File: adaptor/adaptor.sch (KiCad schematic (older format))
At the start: 11 parts, among them P1 CONN_1, P2 nRF24l01, P3 ISP, P4 CONN_1, P5 CONN_1, P6 Clock, P7 Out, P8 In, P9 Serial

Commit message: Add power jack and rj45 connectors to adaptor
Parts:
- removed W1: NoOut, symbol TEST
- removed W2: NoIn, symbol TEST
- added J1, J2: RJ45, symbol RJ45
- added JP1: NoOut, symbol JUMPER
- added JP2: NoIn, symbol JUMPER
- added K1: DC Jack, symbol CONN_3
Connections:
- wire segments 62 -> 84
- no-connect marks 2 -> 7
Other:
- moved on the sheet: P7, P8

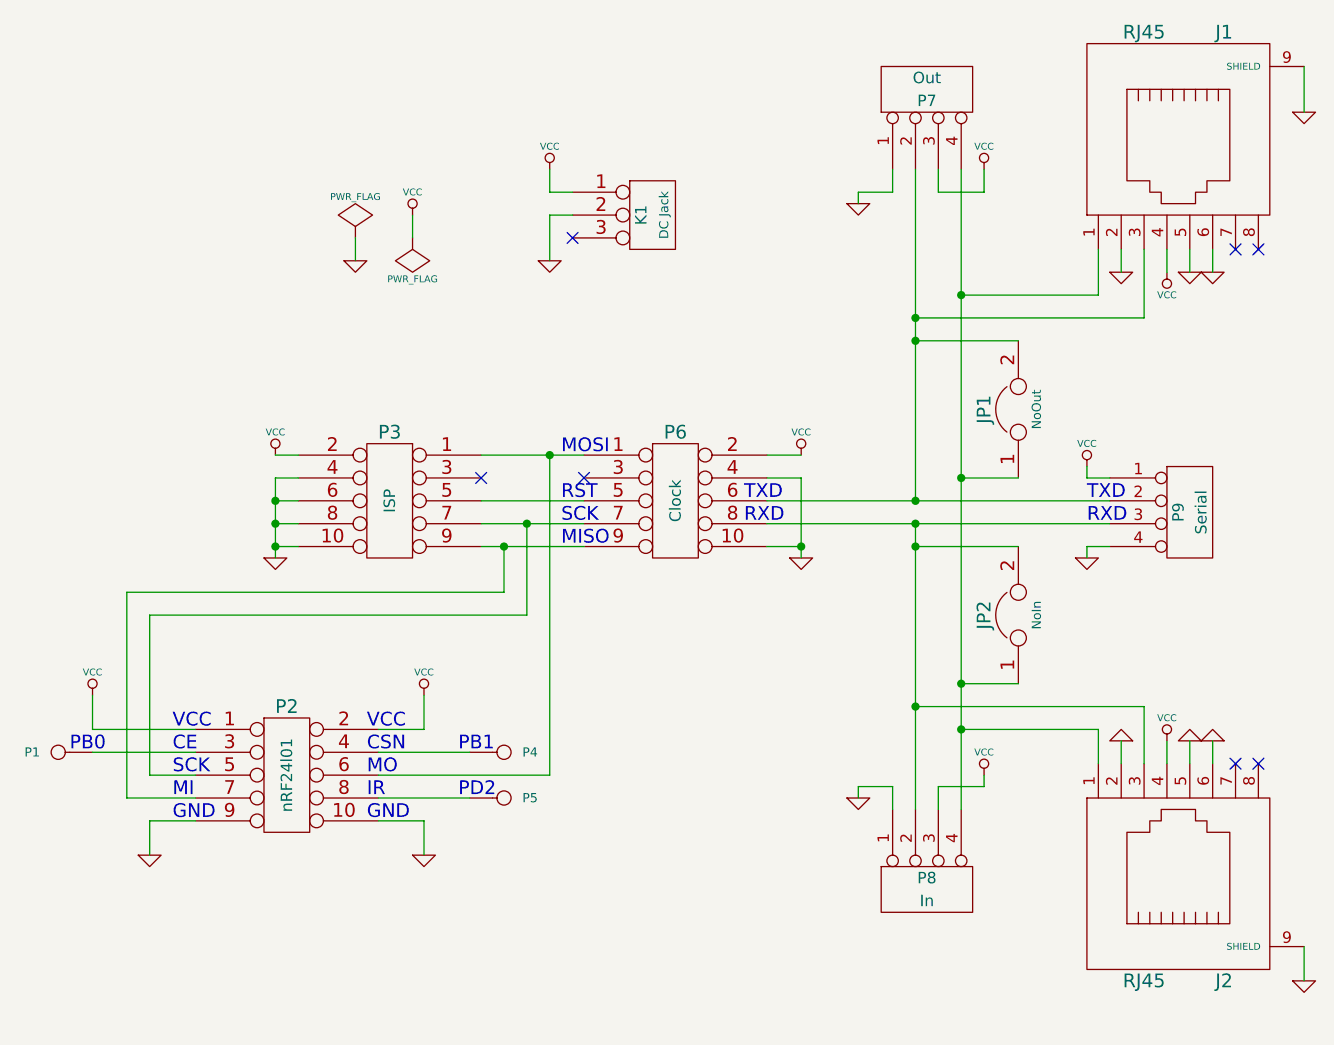
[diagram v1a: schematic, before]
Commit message: Reverse pin numbering on serial conn
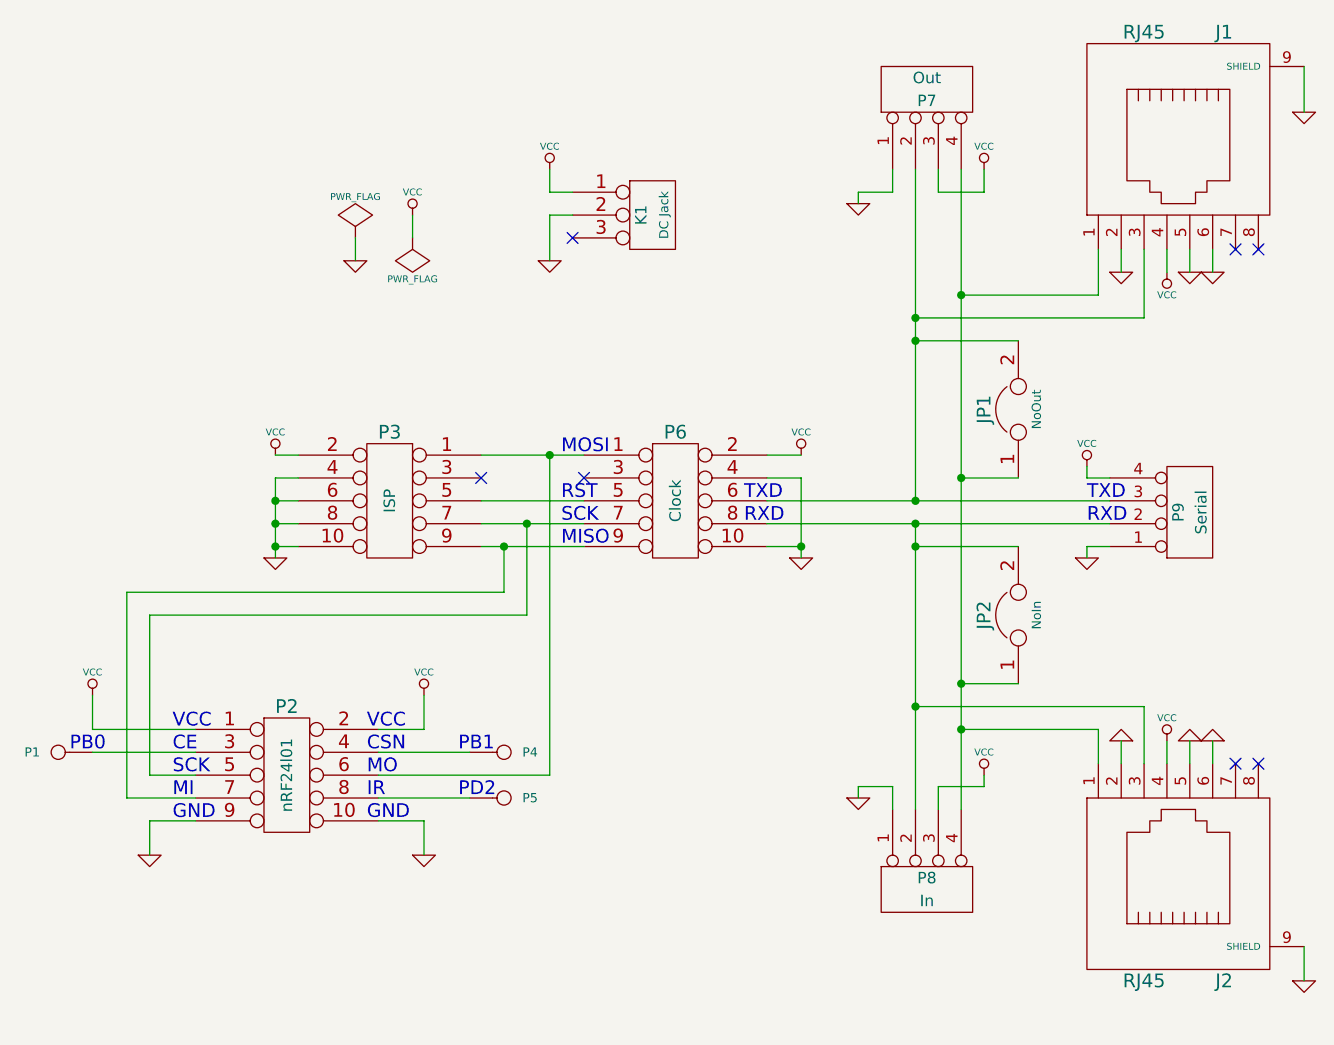
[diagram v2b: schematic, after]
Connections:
- net GND: now also P9.1 (P1); no longer P9.4 (P4)
- net VCC: now also P9.4 (P4); no longer P9.1 (P1)
- net at J1.3, JP1.2, P6.6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: now also P9.3 (P3); no longer P9.2 (P2)
- net at J2.3, JP2.2, P6.8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: now also P9.2 (P2); no longer P9.3 (P3)
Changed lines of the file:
@@
-EESchema Schematic File Version 2  date Sat 12 Jan 2013 20:59:49 EST
+EESchema Schematic File Version 2  date Mon 11 Feb 2013 11:55:31 EST
 LIBS:power
 LIBS:device
@@
 LIBS:contrib
 LIBS:valves
-EELAYER 43  0
+LIBS:adaptor-cache
+EELAYER 25  0
 EELAYER END
 $Descr A4 11700 8267
@@
 Sheet 1 1
 Title ""
-Date "12 jan 2013"
+Date "11 feb 2013"
 Rev ""
 Comp ""
@@
 Connection ~ 5300 3500
 Wire Wire Line
-	5300 2150 5300 4950
+	5300 2150 5300 2700
+Wire Wire Line
+	5300 2700 5300 3500
+Wire Wire Line
+	5300 3500 5300 4400
+Wire Wire Line
+	5300 4400 5300 4600
+Wire Wire Line
+	5300 4600 5300 4950
 Connection ~ 5100 3700
 Wire Wire Line
-	5100 4950 5100 3700
+	5100 4950 5100 4500
+Wire Wire Line
+	5100 4500 5100 3800
+Wire Wire Line
+	5100 3800 5100 3700
 Wire Wire Line
 	5950 3500 5850 3500
@@
 	5850 3500 5850 3450
 Wire Wire Line
-	5950 3600 4450 3600
+	5950 3600 5100 3600
+Wire Wire Line
+	5100 3600 4450 3600
 Wire Wire Line
 	4850 2300 4850 2250
@@
 	2400 3600 2300 3600
 Wire Wire Line
-	3650 3800 3200 3800
+	3650 3800 3300 3800
+Wire Wire Line
+	3300 3800 3200 3800
 Wire Wire Line
 	3650 3600 3200 3600
@@
 	2300 3800 2400 3800
 Wire Wire Line
-	4600 3850 4600 3500
+	4600 3850 4600 3800
+Wire Wire Line
+	4600 3800 4600 3500
 Wire Wire Line
 	4600 3500 4450 3500
@@
 	2300 3400 2400 3400
 Wire Wire Line
-	3650 3400 3200 3400
-Wire Wire Line
-	3650 3700 3200 3700
+	3650 3400 3500 3400
+Wire Wire Line
+	3500 3400 3200 3400
+Wire Wire Line
+	3650 3700 3400 3700
+Wire Wire Line
+	3400 3700 3200 3700
 Wire Wire Line
 	2300 3700 2400 3700
@@
 	2400 3500 2300 3500
 Wire Wire Line
-	2300 3500 2300 3850
+	2300 3500 2300 3600
+Wire Wire Line
+	2300 3600 2300 3700
+Wire Wire Line
+	2300 3700 2300 3800
+Wire Wire Line
+	2300 3800 2300 3850
 Connection ~ 2300 3600
 Wire Wire Line
@@
 	4850 4850 4850 4900
 Wire Wire Line
-	5950 3700 4450 3700
+	5950 3700 5100 3700
+Wire Wire Line
+	5100 3700 4450 3700
 Wire Wire Line
 	5850 3850 5850 3800
@@
 	5850 3800 5950 3800
 Wire Wire Line
-	5100 3600 5100 2150
+	5100 3600 5100 2900
+Wire Wire Line
+	5100 2900 5100 2800
+Wire Wire Line
+	5100 2800 5100 2150
 Connection ~ 5100 3600
 Connection ~ 5100 2900
@@
 F 1 "Serial" V 6350 3650 50  0000 C CNN
 	1    6300 3650
-	1    0    0    -1
-$EndComp
-$Comp
+	1    0    0    1
+$EndComp
+$Comp

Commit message: Move the three gpio pads to a single conn
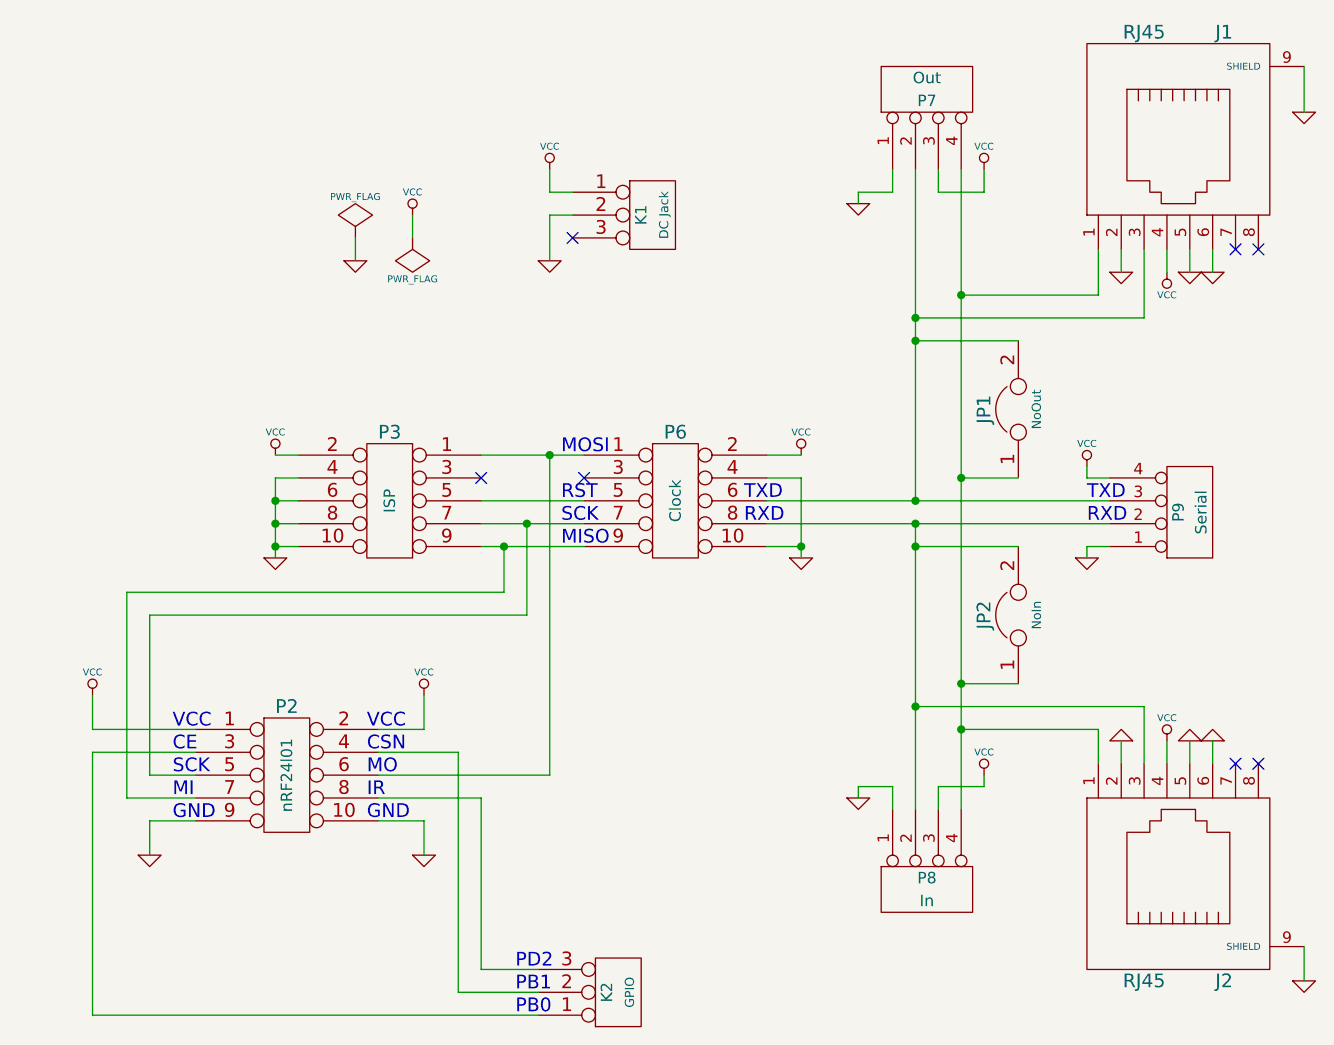
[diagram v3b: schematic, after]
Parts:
- removed P1, P4, P5: CONN_1, symbol CONN_1
- added K2: GPIO, symbol CONN_3
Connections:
- net at P2.3: now also K2.1 (P1)
- net at P2.4: now also K2.2 (PM)
- net at P2.8: now also K2.3 (P3)
